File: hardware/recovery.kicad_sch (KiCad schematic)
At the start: 2 parts, among them J101 3.3V EVAL SUPPLY, J102 CONTROL BOUNDARY

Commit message: Prepare audited RK3566 pin table and resolve recovery resistors and headers
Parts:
- J101: footprint Connector_PinHeader_2.54mm:PinHeader_1x02_P2.54mm_Vertical -> Recovery:Wuerth_61300211121_1x02_P2.54mm_Vertical; MPN (none) -> 61300211121; Manufacturer (none) -> Wuerth Elektronik
- J102: footprint Connector_PinHeader_2.54mm:PinHeader_1x10_P2.54mm_Vertical -> Recovery:Wuerth_61301011121_1x10_P2.54mm_Vertical; MPN (none) -> 61301011121; Manufacturer (none) -> Wuerth Elektronik
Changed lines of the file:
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@@
   (label "ETH_POWER_EN" (at 287.02 134.62 0) (effects (font (size 1.27 1.27)) (justify right bottom)))
   (sheet (at 294.64 91.44) (size 93.98 76.2) (stroke (width 0.254) (type default)) (fill (color 0 0 0 0)) (property "Sheetname" "Recovery outputs" (at 294.64 88.89999999999999 0) (effects (font (size 1.27 1.27)))) (property "Sheetfile" "controls.kicad_sch" (at 294.64 170.18 0) (effects (font (size 1.27 1.27)))) (pin "MODEM_RESET_ASSERT" input (at 294.64 99.06 180) (effects (font (size 1.27 1.27)) (justify left))) (pin "MODEM_OFF_ASSERT" input (at 294.64 104.14 180) (effects (font (size 1.27 1.27)) (justify left))) (pin "ETH_RESET_ASSERT" input (at 294.64 109.22 180) (effects (font (size 1.27 1.27)) (justify left))) (pin "MODEM_RESET_N" output (at 294.64 114.3 180) (effects (font (size 1.27 1.27)) (justify left))) (pin "MODEM_OFF_N" output (at 294.64 119.38 180) (effects (font (size 1.27 1.27)) (justify left))) (pin "ETH_RESET_N" output (at 294.64 124.46000000000001 180) (effects (font (size 1.27 1.27)) (justify left))) (pin "MODEM_POWER_EN" input (at 294.64 129.54 180) (effects (font (size 1.27 1.27)) (justify left))) (pin "ETH_POWER_EN" input (at 294.64 134.62 180) (effects (font (size 1.27 1.27)) (justify left))) (instances (project "recovery" (path "/37b14702-5d54-5543-b96e-899c36eac351" (page "3")))))
-  (symbol (lib_id "Connector_Generic:Conn_01x02") (at 68.58 210.82 0) (unit 1) (in_bom yes) (on_board yes) (dnp no) (property "Reference" "J101" (at 72.39 208.28 0) (effects (font (size 1.27 1.27)) (justify left))) (property "Value" "3.3V EVAL SUPPLY" (at 72.39 210.82 0) (effects (font (size 1.27 1.27)) (justify left))) (property "Footprint" "Connector_PinHeader_2.54mm:PinHeader_1x02_P2.54mm_Vertical" (at 68.58 210.82 0) (effects (font (size 1.27 1.27)) (justify left) (hide yes))) (property "Datasheet" "" (at 68.58 210.82 0) (effects (font (size 1.27 1.27)) (justify left) (hide yes))) (pin "1") (pin "2") (instances (project "recovery" (path "/37b14702-5d54-5543-b96e-899c36eac351" (reference "J101") (unit 1)))))
+  (symbol (lib_id "Connector_Generic:Conn_01x02") (at 68.58 210.82 0) (unit 1) (in_bom yes) (on_board yes) (dnp no) (property "Reference" "J101" (at 72.39 208.28 0) (effects (font (size 1.27 1.27)) (justify left))) (property "Value" "3.3V EVAL SUPPLY" (at 72.39 210.82 0) (effects (font (size 1.27 1.27)) (justify left))) (property "Footprint" "Recovery:Wuerth_61300211121_1x02_P2.54mm_Vertical" (at 68.58 210.82 0) (effects (font (size 1.27 1.27)) (justify left) (hide yes))) (property "Datasheet" "https://www.we-online.com/components/products/datasheet/61300211121.pdf" (at 68.58 210.82 0) (effects (font (size 1.27 1.27)) (justify left) (hide yes))) (pin "1") (pin "2") (instances (project "recovery" (path "/37b14702-5d54-5543-b96e-899c36eac351" (reference "J101") (unit 1)))) (property "MPN" "61300211121" (at 68.58 210.82 0) (effects (font (size 1.27 1.27)) (hide yes))) (property "Manufacturer" "Wuerth Elektronik" (at 68.58 210.82 0) (effects (font (size 1.27 1.27)) (hide yes))))
   (wire (pts (xy 63.5 210.82) (xy 50.8 210.82)) (stroke (width 0) (type default)))
   (symbol (lib_id "power:+3V3") (at 50.8 210.82 0) (unit 1) (in_bom no) (on_board yes) (dnp no) (property "Reference" "#PWR39" (at 54.61 208.28 0) (effects (font (size 1.27 1.27)) (justify left) (hide yes))) (property "Value" "+3V3" (at 52.07 207.01 0) (effects (font (size 1.27 1.27)) (justify left))) (property "Footprint" "" (at 50.8 210.82 0) (effects (font (size 1.27 1.27)) (justify left) (hide yes))) (property "Datasheet" "" (at 50.8 210.82 0) (effects (font (size 1.27 1.27)) (justify left) (hide yes))) (pin "1") (instances (project "recovery" (path "/37b14702-5d54-5543-b96e-899c36eac351" (reference "#PWR39") (unit 1)))))
@@
   (symbol (lib_id "power:PWR_FLAG") (at 45.72 213.36 0) (unit 1) (in_bom no) (on_board yes) (dnp no) (property "Reference" "#FLG43" (at 49.53 210.82000000000002 0) (effects (font (size 1.27 1.27)) (justify left) (hide yes))) (property "Value" "PWR_FLAG" (at 49.53 213.36 0) (effects (font (size 1.27 1.27)) (justify left) (hide yes))) (property "Footprint" "" (at 45.72 213.36 0) (effects (font (size 1.27 1.27)) (justify left) (hide yes))) (property "Datasheet" "" (at 45.72 213.36 0) (effects (font (size 1.27 1.27)) (justify left) (hide yes))) (pin "1") (instances (project "recovery" (path "/37b14702-5d54-5543-b96e-899c36eac351" (reference "#FLG43") (unit 1)))))
   (text "3.3V regulated / current limited.\nNo PoE or unisolated input here." (at 30.48 231.14 0) (effects (font (size 1.27 1.27)) (justify left)))
-  (symbol (lib_id "Connector_Generic:Conn_01x10") (at 203.2 208.28 0) (unit 1) (in_bom yes) (on_board yes) (dnp no) (property "Reference" "J102" (at 207.01 193.04 0) (effects (font (size 1.27 1.27)) (justify left))) (property "Value" "CONTROL BOUNDARY" (at 207.01 195.58 0) (effects (font (size 1.27 1.27)) (justify left))) (property "Footprint" "Connector_PinHeader_2.54mm:PinHeader_1x10_P2.54mm_Vertical" (at 203.2 208.28 0) (effects (font (size 1.27 1.27)) (justify left) (hide yes))) (property "Datasheet" "" (at 203.2 208.28 0) (effects (font (size 1.27 1.27)) (justify left) (hide yes))) (pin "1") (pin "2") (pin "3") (pin "4") (pin "5") (pin "6") (pin "7") (pin "8") (pin "9") (pin "10") (instances (project "recovery" (path "/37b14702-5d54-5543-b96e-899c36eac351" (reference "J102") (unit 1)))))
+  (symbol (lib_id "Connector_Generic:Conn_01x10") (at 203.2 208.28 0) (unit 1) (in_bom yes) (on_board yes) (dnp no) (property "Reference" "J102" (at 207.01 193.04 0) (effects (font (size 1.27 1.27)) (justify left))) (property "Value" "CONTROL BOUNDARY" (at 207.01 195.58 0) (effects (font (size 1.27 1.27)) (justify left))) (property "Footprint" "Recovery:Wuerth_61301011121_1x10_P2.54mm_Vertical" (at 203.2 208.28 0) (effects (font (size 1.27 1.27)) (justify left) (hide yes))) (property "Datasheet" "https://www.we-online.com/components/products/datasheet/61301011121.pdf" (at 203.2 208.28 0) (effects (font (size 1.27 1.27)) (justify left) (hide yes))) (pin "1") (pin "2") (pin "3") (pin "4") (pin "5") (pin "6") (pin "7") (pin "8") (pin "9") (pin "10") (instances (project "recovery" (path "/37b14702-5d54-5543-b96e-899c36eac351" (reference "J102") (unit 1)))) (property "MPN" "61301011121" (at 203.2 208.28 0) (effects (font (size 1.27 1.27)) (hide yes))) (property "Manufacturer" "Wuerth Elektronik" (at 203.2 208.28 0) (effects (font (size 1.27 1.27)) (hide yes))))
   (wire (pts (xy 198.12 198.12) (xy 190.5 198.12)) (stroke (width 0) (type default)))
   (label "MODEM_POWER_EN" (at 190.5 198.12 0) (effects (font (size 1.27 1.27)) (justify right bottom)))

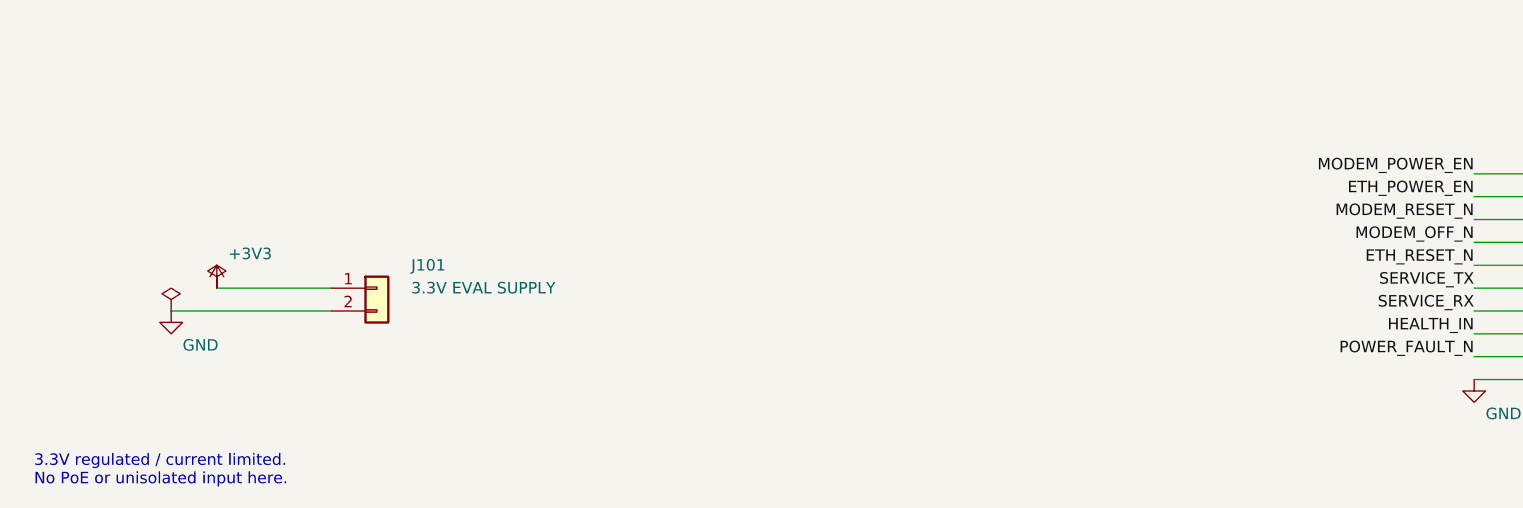
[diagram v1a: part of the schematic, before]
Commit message: Integrate always-on converter into recovery schematic hierarchy
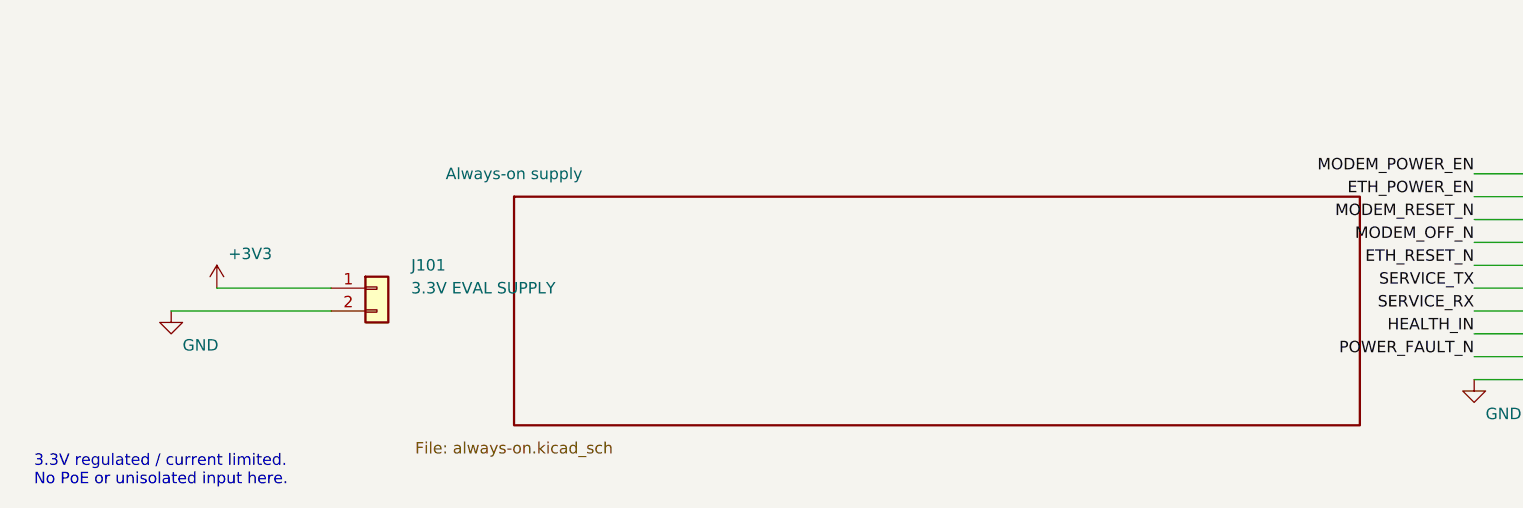
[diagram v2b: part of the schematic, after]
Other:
- added sheet Always-on supply (always-on.kicad_sch)
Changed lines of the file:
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@@
   (wire (pts (xy 63.5 210.82) (xy 50.8 210.82)) (stroke (width 0) (type default)))
   (symbol (lib_id "power:+3V3") (at 50.8 210.82 0) (unit 1) (in_bom no) (on_board yes) (dnp no) (property "Reference" "#PWR39" (at 54.61 208.28 0) (effects (font (size 1.27 1.27)) (justify left) (hide yes))) (property "Value" "+3V3" (at 52.07 207.01 0) (effects (font (size 1.27 1.27)) (justify left))) (property "Footprint" "" (at 50.8 210.82 0) (effects (font (size 1.27 1.27)) (justify left) (hide yes))) (property "Datasheet" "" (at 50.8 210.82 0) (effects (font (size 1.27 1.27)) (justify left) (hide yes))) (pin "1") (instances (project "recovery" (path "/37b14702-5d54-5543-b96e-899c36eac351" (reference "#PWR39") (unit 1)))))
-  (symbol (lib_id "power:PWR_FLAG") (at 50.8 210.82 0) (unit 1) (in_bom no) (on_board yes) (dnp no) (property "Reference" "#FLG40" (at 54.61 208.28 0) (effects (font (size 1.27 1.27)) (justify left) (hide yes))) (property "Value" "PWR_FLAG" (at 54.61 210.82 0) (effects (font (size 1.27 1.27)) (justify left) (hide yes))) (property "Footprint" "" (at 50.8 210.82 0) (effects (font (size 1.27 1.27)) (justify left) (hide yes))) (property "Datasheet" "" (at 50.8 210.82 0) (effects (font (size 1.27 1.27)) (justify left) (hide yes))) (pin "1") (instances (project "recovery" (path "/37b14702-5d54-5543-b96e-899c36eac351" (reference "#FLG40") (unit 1)))))
   (wire (pts (xy 63.5 213.36) (xy 45.72 213.36)) (stroke (width 0) (type default)))
   (symbol (lib_id "power:GND") (at 45.72 213.36 0) (unit 1) (in_bom no) (on_board yes) (dnp no) (property "Reference" "#PWR42" (at 49.53 210.82000000000002 0) (effects (font (size 1.27 1.27)) (justify left) (hide yes))) (property "Value" "GND" (at 46.99 217.17000000000002 0) (effects (font (size 1.27 1.27)) (justify left))) (property "Footprint" "" (at 45.72 213.36 0) (effects (font (size 1.27 1.27)) (justify left) (hide yes))) (property "Datasheet" "" (at 45.72 213.36 0) (effects (font (size 1.27 1.27)) (justify left) (hide yes))) (pin "1") (instances (project "recovery" (path "/37b14702-5d54-5543-b96e-899c36eac351" (reference "#PWR42") (unit 1)))))
-  (symbol (lib_id "power:PWR_FLAG") (at 45.72 213.36 0) (unit 1) (in_bom no) (on_board yes) (dnp no) (property "Reference" "#FLG43" (at 49.53 210.82000000000002 0) (effects (font (size 1.27 1.27)) (justify left) (hide yes))) (property "Value" "PWR_FLAG" (at 49.53 213.36 0) (effects (font (size 1.27 1.27)) (justify left) (hide yes))) (property "Footprint" "" (at 45.72 213.36 0) (effects (font (size 1.27 1.27)) (justify left) (hide yes))) (property "Datasheet" "" (at 45.72 213.36 0) (effects (font (size 1.27 1.27)) (justify left) (hide yes))) (pin "1") (instances (project "recovery" (path "/37b14702-5d54-5543-b96e-899c36eac351" (reference "#FLG43") (unit 1)))))
   (text "3.3V regulated / current limited.\nNo PoE or unisolated input here." (at 30.48 231.14 0) (effects (font (size 1.27 1.27)) (justify left)))
   (symbol (lib_id "Connector_Generic:Conn_01x10") (at 203.2 208.28 0) (unit 1) (in_bom yes) (on_board yes) (dnp no) (property "Reference" "J102" (at 207.01 193.04 0) (effects (font (size 1.27 1.27)) (justify left))) (property "Value" "CONTROL BOUNDARY" (at 207.01 195.58 0) (effects (font (size 1.27 1.27)) (justify left))) (property "Footprint" "Recovery:Wuerth_61301011121_1x10_P2.54mm_Vertical" (at 203.2 208.28 0) (effects (font (size 1.27 1.27)) (justify left) (hide yes))) (property "Datasheet" "https://www.we-online.com/components/products/datasheet/61301011121.pdf" (at 203.2 208.28 0) (effects (font (size 1.27 1.27)) (justify left) (hide yes))) (pin "1") (pin "2") (pin "3") (pin "4") (pin "5") (pin "6") (pin "7") (pin "8") (pin "9") (pin "10") (instances (project "recovery" (path "/37b14702-5d54-5543-b96e-899c36eac351" (reference "J102") (unit 1)))) (property "MPN" "61301011121" (at 203.2 208.28 0) (effects (font (size 1.27 1.27)) (hide yes))) (property "Manufacturer" "Wuerth Elektronik" (at 203.2 208.28 0) (effects (font (size 1.27 1.27)) (hide yes))))
@@
   (text "Service UART / health / fault inputs:\n3.3V only. Add powered-off-safe translation\nwhen target voltage requires it.\nService UART must not back-power target.\n\nNo MCU modem-session interface is implemented." (at 271.78 210.82 0) (effects (font (size 1.27 1.27)) (justify left)))
   (sheet_instances (path "/" (page "1")))
+(sheet (at 83.82 200.66) (size 93.98 25.4) (stroke (width 0.254) (type default)) (fill (color 0 0 0 0)) (property "Sheetname" "Always-on supply" (at 83.82 198.12 0) (effects (font (size 1.27 1.27)))) (property "Sheetfile" "always-on.kicad_sch" (at 83.82 228.6 0) (effects (font (size 1.27 1.27)))) (instances (project "recovery" (path "/37b14702-5d54-5543-b96e-899c36eac351" (page "4")))))
 )

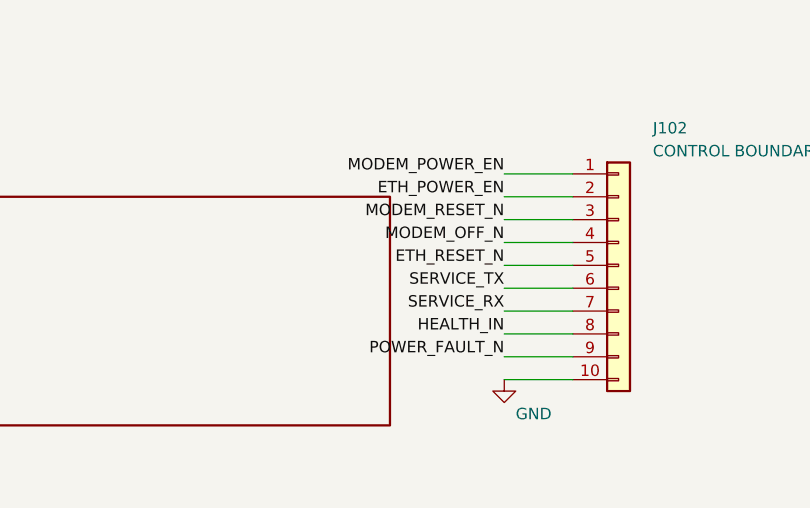
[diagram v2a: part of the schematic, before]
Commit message: Connect always-on power-good to recovery fault input
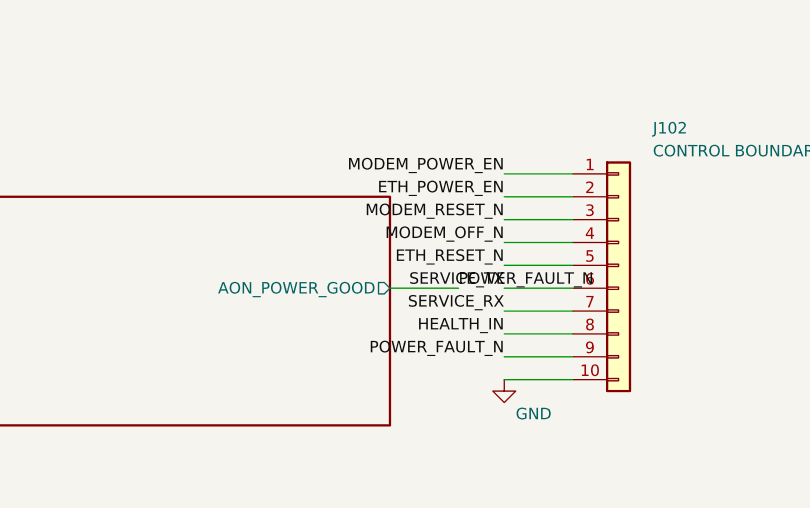
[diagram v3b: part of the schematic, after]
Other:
- sheet Always-on supply ports: added AON_POWER_GOOD; removed none
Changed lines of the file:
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@@
   (text "Service UART / health / fault inputs:\n3.3V only. Add powered-off-safe translation\nwhen target voltage requires it.\nService UART must not back-power target.\n\nNo MCU modem-session interface is implemented." (at 271.78 210.82 0) (effects (font (size 1.27 1.27)) (justify left)))
   (sheet_instances (path "/" (page "1")))
-(sheet (at 83.82 200.66) (size 93.98 25.4) (stroke (width 0.254) (type default)) (fill (color 0 0 0 0)) (property "Sheetname" "Always-on supply" (at 83.82 198.12 0) (effects (font (size 1.27 1.27)))) (property "Sheetfile" "always-on.kicad_sch" (at 83.82 228.6 0) (effects (font (size 1.27 1.27)))) (instances (project "recovery" (path "/37b14702-5d54-5543-b96e-899c36eac351" (page "4")))))
+(sheet (at 83.82 200.66) (size 93.98 25.4) (stroke (width 0.254) (type default)) (fill (color 0 0 0 0)) (property "Sheetname" "Always-on supply" (at 83.82 198.12 0) (effects (font (size 1.27 1.27)))) (property "Sheetfile" "always-on.kicad_sch" (at 83.82 228.6 0) (effects (font (size 1.27 1.27)))) (pin "AON_POWER_GOOD" output (at 177.8 210.82 0) (effects (font (size 1.27 1.27)) (justify right))) (instances (project "recovery" (path "/37b14702-5d54-5543-b96e-899c36eac351" (page "4")))))
+(wire (pts (xy 177.8 210.82) (xy 185.42 210.82)) (stroke (width 0) (type default)))
+(label "POWER_FAULT_N" (at 185.42 210.82 0) (effects (font (size 1.27 1.27)) (justify left bottom)))
 )
